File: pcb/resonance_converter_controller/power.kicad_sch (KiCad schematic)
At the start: 107 parts, among them Q1 FDMC8032L, Q2 FDMC8032L, Q3 SiR696DP, SW1 SW_SPST, U1 BQ25792RQMR, U2 TPS55289RYQR, U3 TPS54240DRC, U4 TPS73733DCQR, U6 LP5907MFX-3.3

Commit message: Update conector in som
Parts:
- added R71: R, Resistor_SMD:R_2512_6332Metric, symbol Device:R
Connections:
- net VOUT: now also R71.2
- net VPP: now also R71.1
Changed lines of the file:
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@@
 	)
 	(junction
+		(at 116.84 213.36)
+		(diameter 0)
+		(color 0 0 0 0)
+	)
+	(junction
 		(at 228.6 290.83)
 		(diameter 0)
@@
 	(wire
 		(pts
-			(xy 83.82 213.36) (xy 127 213.36)
+			(xy 83.82 213.36) (xy 116.84 213.36)
 		)
 		(stroke
@@
 	(wire
 		(pts
+			(xy 307.34 196.85) (xy 307.34 220.98)
+		)
+		(stroke
+			(width 0)
+			(type default)
+		)
+	)
+	(wire
+		(pts
 			(xy 83.82 30.48) (xy 90.17 30.48)
 		)
@@
 	(wire
 		(pts
+			(xy 143.51 196.85) (xy 116.84 196.85)
+		)
+		(stroke
+			(width 0)
+			(type default)
+		)
+	)
+	(wire
+		(pts
 			(xy 387.35 337.82) (xy 400.05 337.82)
 		)
@@
 	(wire
 		(pts
+			(xy 116.84 196.85) (xy 116.84 213.36)
+		)
+		(stroke
+			(width 0)
+			(type default)
+		)
+	)
+	(wire
+		(pts
 			(xy 234.95 220.98) (xy 234.95 227.33)
 		)
@@
 	(wire
 		(pts
+			(xy 151.13 196.85) (xy 307.34 196.85)
+		)
+		(stroke
+			(width 0)
+			(type default)
+		)
+	)
+	(wire
+		(pts
 			(xy 83.82 219.71) (xy 83.82 213.36)
 		)
@@
 	(wire
 		(pts
+			(xy 116.84 213.36) (xy 127 213.36)
+		)
+		(stroke
+			(width 0)
+			(type default)
+		)
+	)
+	(wire
+		(pts
 			(xy 132.08 30.48) (xy 132.08 36.83)
 		)
@@
 					(unit 1)
 				)
+			)
+		)
+	)
+	(symbol
+		(lib_id "Device:R")
+		(at 147.32 196.85 90)
+		(unit 1)
+		(exclude_from_sim no)
+		(in_bom yes)
+		(on_board yes)
+		(dnp yes)
+		(fields_autoplaced yes)
+		(property "Reference" "R71"
+			(at 147.32 190.5 90)
+			(effects
+				(font
+					(size 1.27 1.27)
+				)
+			)
+		)
+		(property "Value" "R"
+			(at 147.32 193.04 90)
+			(effects
+				(font
+					(size 1.27 1.27)
+				)
+			)
+		)
+		(property "Footprint" "Resistor_SMD:R_2512_6332Metric"
+			(at 147.32 198.628 90)
+			(effects
+				(font
+					(size 1.27 1.27)
+				)
+				(hide yes)
+			)
+		)
+		(property "Datasheet" "~"
+			(at 147.32 196.85 0)
+			(effects
+				(font
+					(size 1.27 1.27)
+				)
+				(hide yes)
+			)
+		)
+		(property "Description" "Resistor"
+			(at 147.32 196.85 0)
+			(effects
+				(font
+					(size 1.27 1.27)
+				)
+				(hide yes)
+			)
+		)
+		(pin "1"
+		)
+		(pin "2"
+		)
+		(instances
+			(project "resoncance_converter_controller"
+				(path "/834b5629-1e5f-4005-abd6-bf54830363e9/8125c579-eefb-4931-838b-39d668710a66"
+					(reference "R71")
+					(unit 1)
+				)

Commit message: First routing without testpoints
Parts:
- D4: footprint Diode_SMD:D_SMC -> Diode_SMD:D_SMB
- R71: footprint Resistor_SMD:R_2512_6332Metric -> Resistor_SMD:R_1206_3216Metric
- SW1: footprint Button_Switch_SMD:SW_Push_1P1T_NO_CK_KSC6xxJ -> Button_Switch_SMD:SW_SPST_EVQPE1
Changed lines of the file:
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@@
 			)
 		)
-		(property "Footprint" "Diode_SMD:D_SMC"
+		(property "Footprint" "Diode_SMD:D_SMB"
 			(at 192.405 294.64 0)
 			(effects
@@
 			)
 		)
-		(property "Footprint" "Button_Switch_SMD:SW_Push_1P1T_NO_CK_KSC6xxJ"
+		(property "Footprint" "Button_Switch_SMD:SW_SPST_EVQPE1"
 			(at 118.11 128.27 0)
 			(effects
@@
 			)
 		)
-		(property "Footprint" "Resistor_SMD:R_2512_6332Metric"
+		(property "Footprint" "Resistor_SMD:R_1206_3216Metric"
 			(at 147.32 198.628 90)
 			(effects

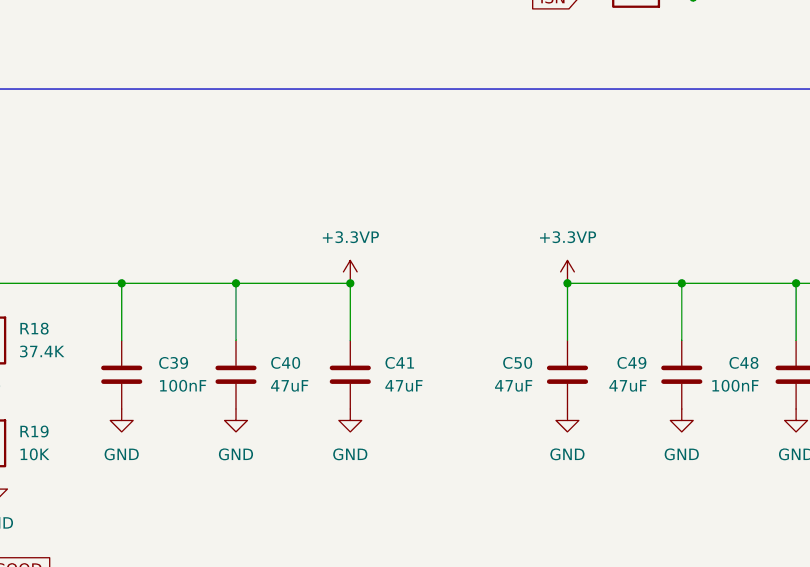
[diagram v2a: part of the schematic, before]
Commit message: Add reset handler buffer for dac and led
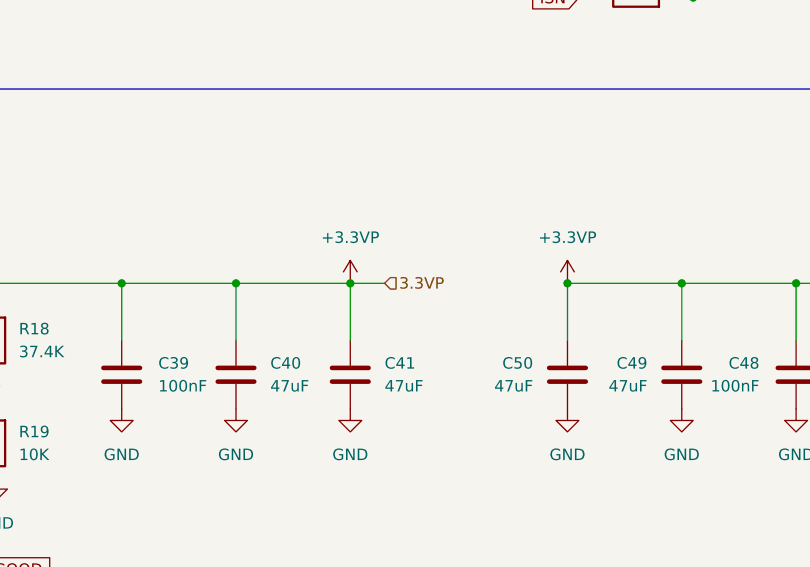
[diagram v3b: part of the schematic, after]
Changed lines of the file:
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@@
+	(wire
+		(pts
+			(xy 257.81 290.83) (xy 254 290.83)
+		)
+		(stroke
+			(width 0)
+			(type default)
+		)
+	)
 	(wire
 		(pts
@@
 		)
 	)
+	(hierarchical_label "3.3VP"
+		(shape input)
+		(at 257.81 290.83 0)
+		(effects
+			(font
+				(size 1.27 1.27)
+			)
+			(justify left)
+		)
+	)

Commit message: Add io panel and fix controller pcb
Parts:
- removed L2: 4.7uH, Inductor_SMD:L_6.3x6.3_H3, symbol Device:L
- added C100: 47nF, Capacitor_SMD:C_0402_1005Metric, symbol Device:C
- added L2: ASPI-8030LR-4R7M-T, ASPI-8030LR-4R7M-T:IND_ASPI-8030LR-4R7M-T, symbol ASPI-8030LR-4R7M-T:ASPI-8030LR-4R7M-T
- L1: footprint Inductor_SMD:L_6.3x6.3_H3 -> Inductor_SMD:L_10.4x10.4_H4.8
- L3: footprint Inductor_SMD:L_6.3x6.3_H3 -> Capacitor_SMD:C_2220_5750Metric
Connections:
- net GND: now also C100.2
- net at C23.2, U2.8 (SW1): now also L2.1
- net at C24.1, U2.10 (SW2): now also L2.2
- net /QON: now reaches SW1.2 (B), U1.12 (~{QON})
- net at R12.2, U1.18 (BATP): now also C100.1
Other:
- moved on the sheet: SW1
